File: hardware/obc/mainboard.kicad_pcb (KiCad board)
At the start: 6 copper layers, 95.9 x 90.2 mm, 213 parts, among them J101 Conn_02x20_Odd_Even, J301 USB_C_Receptacle_USB2.0, J302 Conn_High-Rel_4S2P, J303 Conn_01x06, J304 Conn_High-Rel_6P, J305 Conn_01x05, J601 Conn_01x08_Socket, J602 SMA RA Connector, J603 SMA RA Connector, J604 SMA RA Connector, Q201 BSS138DWQ-7, Q202 BSS138DWQ-7, Q203 MBT2222ADW1T1, Q204 MBT2222ADW1T1, Q205 BSS138DWQ-7, Q206 BSS138DWQ-7, Q207 MBT2222ADW1T1, Q208 MBT2222ADW1T1, Q209 MMDT2907, Q401 MBT2222ADW1T1, Q402 MBT2222ADW1T1, Q403 IRLML2803, Q404 IRF7406PbF, Q501 MMBT2222AT, Q502 IRLML2803, Q503 IRLML2803, Q504 IRLML2803, Q505 IRF7406PbF, Q506 IRF7406PbF, Q507 IRF7406PbF, U101 MAX706RESA, U102 ATSAMD51J20A-AU, U103 BMI088, U301 Mem_MT29F4G01ABAFDWB, U302 Mem_MT29F4G01ABAFDWB, U401 TPS7A4501DCQT, U402 LTC4121, U403 TPS54226PWPRPWP14_2P31X2P46-L, U404 ADM1176-1ARMZ-R7, U405 BQ25886RGER, U501 PE014006, U601 RFM98PW, U602 S1216V8, U603 GP2S1+, Y101 32.768kHz

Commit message: obc: begun formal layout
Organized the components of the first two schematic pages into formal layout and switched out connector components. Introduced step files for previously developed footprints.
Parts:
- added C118: 0.1uF, Capacitor_SMD:C_0603_1608Metric, F.Cu at (148.0, 111.6)
- added C119: 0.1uF, Capacitor_SMD:C_0603_1608Metric, F.Cu at (160.8, 105.2)
- added C120: 0.1uF, Capacitor_SMD:C_0603_1608Metric, F.Cu at (151.2, 91.6)
- J303: footprint Connector_PinHeader_2.54mm:PinHeader_1x06_P2.54mm_Vertical -> Connector_PinHeader_2.54mm:PinHeader_1x06_P2.54mm_Horizontal
- J304: footprint SSE_Footprints:Harwin_M300-MV30645M1_6P_P3.0mm_Vertical -> SSE_Footprints:MMCX-6_UMPT-06-01-L-RA-WT-TR_P2.0mm
- moved J301 222.8 mm to (250.8, 40.8), turned to 90 degrees
- moved C303 209.9 mm to (242.6, 35.5), turned to 180 degrees
- moved R307 208.4 mm to (242.5, 46.8), turned to 0 degrees
- moved R304 208.1 mm to (242.5, 41.1), turned to 0 degrees
- moved R303 208.0 mm to (242.5, 44.0), turned to 0 degrees
- moved R306 207.9 mm to (242.5, 38.4), turned to 0 degrees
- moved R112 130.0 mm to (110.8, 143.4)
- moved R231 122.9 mm to (244.0, 118.8), turned to 0 degrees
- moved R229 121.3 mm to (244.0, 115.4), turned to 0 degrees
- moved H101 120.5 mm to (191.7, 140.8), turned to 180 degrees
- moved R230 120.4 mm to (244.0, 121.6), turned to 0 degrees
- moved R110 119.8 mm to (186.8, 140.8), turned to 180 degrees
- moved H103 115.5 mm to (106.0, 143.3), turned to 180 degrees
- moved H102 114.6 mm to (191.7, 67.1), turned to 180 degrees
- moved H104 110.7 mm to (106.0, 63.3), turned to 180 degrees
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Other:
- board text added: "+X"
- board text added: "+Y"
- board text added: "+Z"

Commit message: obc: formal placement and 3D models entered
Placed components of onto board, orienting them for ease of trace creation. Entered 3D models of footprints into KiCad for design verification and aesthetics.
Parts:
- J304, U501: moved to B.Cu
- U404: value ADM1176-1ARMZ-R7 -> RM_10
- moved J302 242.0 mm to (266.4, 39.6)
- moved C304 221.1 mm to (260.4, 39.3), turned to 180 degrees
- moved C305 218.6 mm to (260.4, 42.1), turned to 180 degrees
- moved J304 161.0 mm to (207.1, 81.5), turned to -90 degrees
- moved J303 157.4 mm to (186.4, 74.5), turned to 0 degrees
- moved R510 147.0 mm to (152.8, 78.4), turned to 180 degrees
- moved JP509 146.0 mm to (142.0, 75.1), turned to 90 degrees
- moved R507 145.4 mm to (152.8, 81.2), turned to 0 degrees
- moved Q504 144.7 mm to (148.9, 79.8), turned to 180 degrees
- moved D402 143.3 mm to (194.3, 104.0), turned to 180 degrees
- moved R504 143.0 mm to (148.8, 84.0), turned to 180 degrees
- moved R430 140.9 mm to (189.8, 104.0), turned to 180 degrees
- moved Q507 139.8 mm to (142.0, 80.8), turned to 180 degrees
- moved JP508 135.0 mm to (135.0, 75.1), turned to 90 degrees
- moved JP507 130.4 mm to (127.9, 65.7), turned to 90 degrees
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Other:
- outline, holes or cut-outs redrawn

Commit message: obc: component reorganization
Blanket shrunk silk text, edited connector placement, switched out molex connectors, entered step files, and reorganized to increase area-efficiency.
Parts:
- JP501, JP502, JP503, JP504, JP505, JP506: footprint mainboard:MOLEX-1X3_LOCK -> SSE_Footprints:CONN_22-11-2032_MOL
- JP507, JP508, JP509: footprint mainboard:MOLEX-1X3_LOCK -> SSE_Footprints:CONN_22-11-2032_MOL; moved to B.Cu
- U404: value RM_10 -> ADM1176-1ARMZ-R7
- moved C601 74.2 mm to (204.4, 137.2)
- moved Q209 73.5 mm to (141.1, 119.6)
- moved R225 70.7 mm to (146.0, 125.2)
- moved R226 70.7 mm to (146.0, 122.4)
- moved R228 67.0 mm to (141.2, 126.0)
- moved R227 67.0 mm to (141.2, 123.2)
- moved U601 61.4 mm to (166.4, 129.8)
- moved C407 49.9 mm to (150.7, 171.7)
- moved L401 49.9 mm to (154.7, 171.3)
- moved U403 49.9 mm to (143.2, 172.4)
- moved C410 49.9 mm to (135.9, 172.9)
- moved C412 49.9 mm to (135.9, 170.1)
- moved R409 49.9 mm to (140.3, 166.1)
- moved R412 49.9 mm to (143.1, 166.1)
- moved R413 49.8 mm to (140.4, 182.6)
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
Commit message: obc: preliminary layout complete
Finished preliminary layout of components onto pcb. Entered revised SMA connector into design, however, there is confusion with regards to board cutouts.
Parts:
- J602, J603, J604: footprint Connector_Coaxial:SMA_Amphenol_132289_EdgeMount -> SSE_Footprints:SAMTEC_MMCXV-J-P-HF-ST-EM1
- moved J602 182.8 mm to (183.6, 116.6), turned to -90 degrees
- moved J603 180.3 mm to (183.6, 123.8), turned to -90 degrees
- moved J604 159.6 mm to (183.6, 131.2), turned to -90 degrees
- moved C304 112.4 mm to (160.8, 91.2)
- moved C305 112.3 mm to (160.8, 94.0)
- moved J302 109.2 mm to (167.8, 86.4)
- moved R229 93.8 mm to (152.8, 137.6), turned to 90 degrees
- moved R231 90.4 mm to (155.6, 137.6), turned to 90 degrees
- moved R230 87.1 mm to (158.4, 137.6), turned to 90 degrees
- moved R602 65.8 mm to (160.8, 88.4)
- moved U603 52.9 mm to (170.0, 118.3)
- moved C401 50.7 mm to (168.3, 126.4)
- moved C402 50.6 mm to (165.5, 126.4)
- moved C413 50.5 mm to (164.0, 134.3)
- moved R413 50.5 mm to (155.6, 134.3)
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
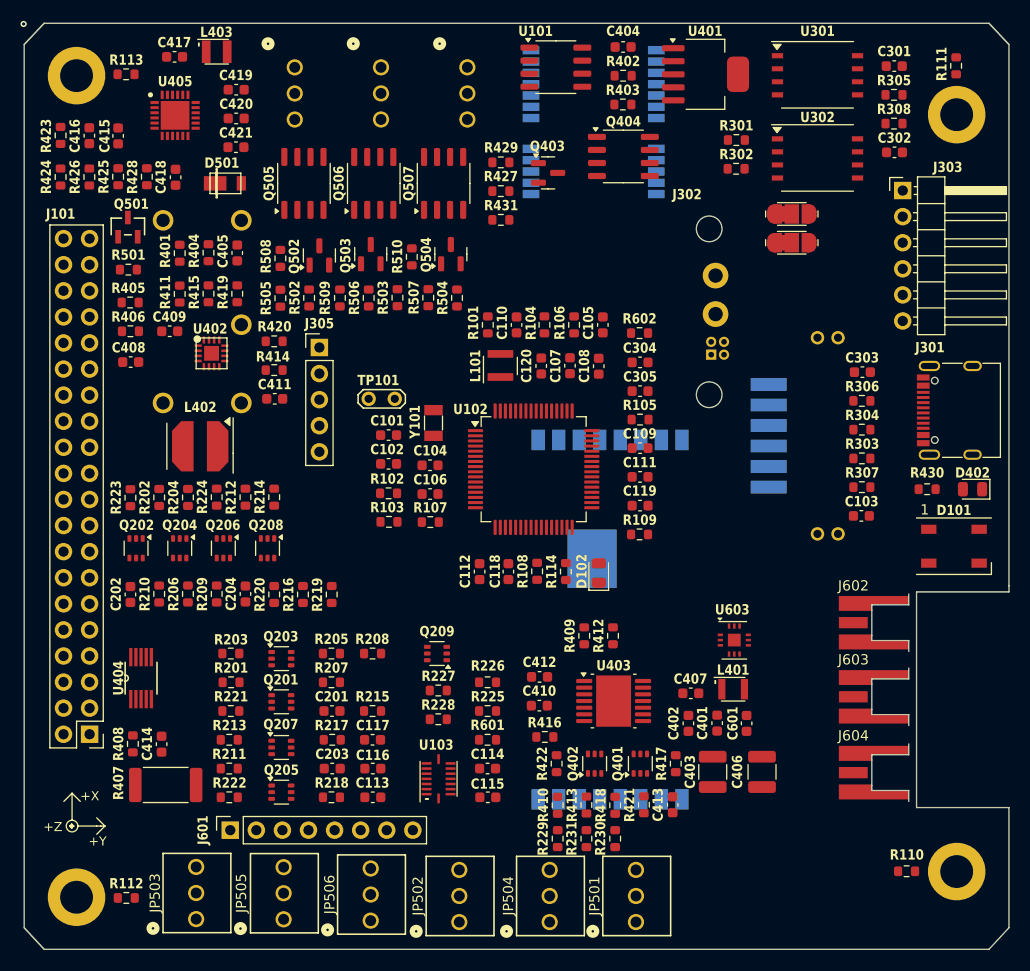
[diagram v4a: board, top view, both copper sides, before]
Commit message: obc: Update board outline and MMCXV 3d model
The model was upside down; the board edge lines were not connected.
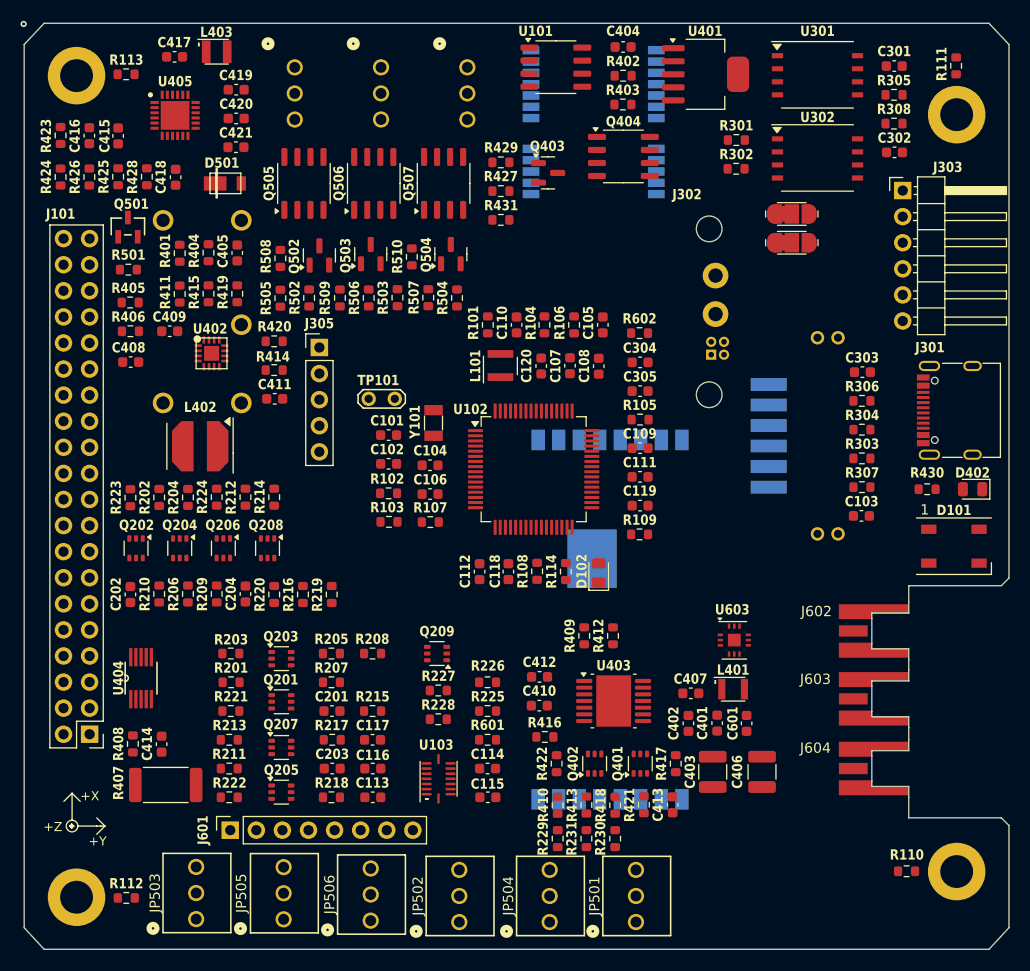
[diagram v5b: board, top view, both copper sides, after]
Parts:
- moved J602 0.80 mm to (183.6, 117.4)
- moved J604 0.40 mm to (183.6, 130.8)
- moved J603 0.20 mm to (183.6, 124.0)
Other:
- outline, holes or cut-outs redrawn
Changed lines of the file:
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@@
 	(footprint "SSE_Footprints:SAMTEC_MMCXV-J-P-HF-ST-EM1"
 		(layer "F.Cu")
-		(at 183.6 123.8125 -90)
+		(at 183.6 124.0125 -90)
 		(property "Reference" "J603"
-			(at -3.6125 2 180)
+			(at -1.9125 5.7 180)
 			(layer "F.SilkS")
 			(effects
@@
 			)
 		)
-		(property ki_fp_filters "*BNC* *SMA* *SMB* *SMC* *Cinch* *LEMO* *UMRF* *MCX* *U.FL*")
-		(sheetname "RF and GPS")
-		(sheetfile "RF_and_GPS.kicad_sch")
 		(attr smd)
 		(fp_poly
@@
 		(model "MMCXV-J-P-HF-ST-EM1.step"
 			(offset
-				(xyz 0 -0.5 0)
+				(xyz 0 -0.15 0.4)
 			)
 			(scale
@@
 			)
 			(rotate
-				(xyz 0 0 0)
+				(xyz 0 180 0)
 			)
 		)
@@
 		(tags "Through hole pin header THT 1x05 2.54mm single row")
 		(property "Reference" "J305"
-			(at 0 -2.33 360)
+			(at 0 -2.33 0)
 			(layer "F.SilkS")
 			(effects
@@
 		)
 		(property "Value" "Conn_01x05"
-			(at 0 12.49 360)
+			(at 0 12.49 0)
 			(layer "F.Fab")
 			(effects
@@
 		(tags "resistor")
 		(property "Reference" "R230"
-			(at 0 -1.43 270)
+			(at 0 -1.43 -90)
 			(layer "F.SilkS")
 			(effects
@@
 		)
 		(property "Value" "0"
-			(at 0 1.43 270)
+			(at 0 1.43 -90)
 			(layer "F.Fab")
 			(effects
@@
 		)
 		(fp_text user "${REFERENCE}"
-			(at 0 0 270)
+			(at 0 0 -90)
 			(layer "F.Fab")
 			(effects
@@
 		(tags "resistor")
 		(property "Reference" "R231"
-			(at 0 -1.43 270)
+			(at 0 -1.43 -90)
 			(layer "F.SilkS")
 			(effects
@@
 		)
 		(property "Value" "0"
-			(at 0 1.43 270)
+			(at 0 1.43 -90)
 			(layer "F.Fab")
 			(effects
@@
 		)
 		(fp_text user "${REFERENCE}"
-			(at 0 0 270)
+			(at 0 0 -90)
 			(layer "F.Fab")
 			(effects
@@
 		(tags "resistor")
 		(property "Reference" "R229"
-			(at 0 -1.43 270)
+			(at 0 -1.43 -90)
 			(layer "F.SilkS")
 			(effects
@@
 		)
 		(property "Value" "0"
-			(at 0 1.43 270)
+			(at 0 1.43 -90)
 			(layer "F.Fab")
 			(effects
@@
 		)
 		(fp_text user "${REFERENCE}"
-			(at 0 0 270)
+			(at 0 0 -90)
 			(layer "F.Fab")
 			(effects
@@
 	(footprint "SSE_Footprints:SAMTEC_MMCXV-J-P-HF-ST-EM1"
 		(layer "F.Cu")
-		(at 183.6 131.2 -90)
+		(at 183.6 130.8 -90)
 		(property "Reference" "J604"
-			(at -3.6 2 180)
+			(at -2 5.7 180)
 			(layer "F.SilkS")
 			(effects
@@
 			)
 		)
-		(property ki_fp_filters "*BNC* *SMA* *SMB* *SMC* *Cinch* *LEMO* *UMRF* *MCX* *U.FL*")
-		(sheetname "RF and GPS")
-		(sheetfile "RF_and_GPS.kicad_sch")
 		(attr smd)
 		(fp_poly
@@
 		(model "MMCXV-J-P-HF-ST-EM1.step"
 			(offset
-				(xyz 0 -0.5 0)
+				(xyz 0 -0.15 0.4)
 			)
 			(scale
@@
 			)
 			(rotate
-				(xyz 0 0 0)
+				(xyz 0 180 0)
 			)
 		)
@@
 	(footprint "SSE_Footprints:SAMTEC_MMCXV-J-P-HF-ST-EM1"
 		(layer "F.Cu")
-		(at 183.6 116.6 -90)
+		(at 183.6 117.4 -90)
 		(property "Reference" "J602"
-			(at -3.6 2 180)
+			(at -1.9 5.6 180)
 			(layer "F.SilkS")
 			(effects
@@
 			)
 		)
-		(property ki_fp_filters "*BNC* *SMA* *SMB* *SMC* *Cinch* *LEMO* *UMRF* *MCX* *U.FL*")
-		(sheetname "RF and GPS")
-		(sheetfile "RF_and_GPS.kicad_sch")
 		(attr smd)
 		(fp_poly
@@
 		(model "MMCXV-J-P-HF-ST-EM1.step"
 			(offset
-				(xyz 0 -0.5 0)
+				(xyz 0 -0.15 0.4)
 			)
 			(scale
@@
 			)
 			(rotate
-				(xyz 0 0 0)
+				(xyz 0 180 0)
 			)
 		)
@@
 		(tags "resistor")
 		(property "Reference" "R602"
-			(at 0 -1.4 360)
+			(at 0 -1.4 0)
 			(layer "F.SilkS")
 			(effects
@@
 		)
 		(property "Value" "10k"
-			(at 0 1.43 360)
+			(at 0 1.43 0)
 			(layer "F.Fab")
 			(effects
@@
 		)
 		(fp_text user "${REFERENCE}"
-			(at 0 0 360)
+			(at 0 0 0)
 			(layer "F.Fab")
 			(effects
@@
 		(at 158.4 116.4 90)
 		(property "Reference" "U601"
-			(at 1.016 2.667 270)
+			(at 1.016 2.667 -90)
 			(layer "B.SilkS")
 			(hide yes)
@@
 		)
 		(property "Value" "RFM98PW"
-			(at -4.318 -7.6835 270)
+			(at -4.318 -7.6835 -90)
 			(layer "B.SilkS")
 			(hide yes)
@@
 		)
 		(fp_text user "RADIO 2"
-			(at 5.08 6.1595 270)
+			(at 5.08 6.1595 -90)
 			(layer "B.SilkS")
 			(hide yes)
@@
 	)
 	(gr_line
-		(start 196.745 134.6)
+		(start 196.745 136.345)
 		(end 196.745 146.3)
 		(stroke
@@
 	)
 	(gr_line
+		(start 186.99 133.6)
+		(end 186.99 135.6)
+		(stroke
+			(width 0.1)
+			(type default)
+		)
+		(layer "Edge.Cuts")
+	)
+	(gr_line
 		(start 100.855 146.3)
 		(end 100.855 60.3)
@@
 	(gr_line
 		(start 102.8 148.4)
-		(end 100.855 146.3)
+		(end 100.854984 146.300015)
 		(stroke
-			(width 0.15)
+			(width 0.1)
 			(type default)
 		)
@@
 	)
 	(gr_line
-		(start 187.745 134.6)
-		(end 187.745 113.6)
+		(start 186.99 113)
+		(end 186.99 114.6)
 		(stroke
 			(width 0.1)
@@
 	)
 	(gr_line
-		(start 187.745 113.6)
-		(end 196.745 113.6)
+		(start 186.99 113)
+		(end 196 113)
 		(stroke
 			(width 0.1)
@@
 	(gr_line
 		(start 196.745 60.3)
-		(end 196.745 113)
+		(end 196.745 112.255)
+		(stroke
+			(width 0.1)
+			(type default)
+		)
+		(layer "Edge.Cuts")
+	)
+	(gr_line
+		(start 186.99 126.8125)
+		(end 186.99 128)
 		(stroke
 			(width 0.1)
@@
 	)
 	(gr_line
-		(start 187.745 134.6)
-		(end 196.745 134.6)
+		(start 186.99 135.6)
+		(end 196 135.6)
+		(stroke
+			(width 0.1)
+			(type default)
+		)
+		(layer "Edge.Cuts")
+	)
+	(gr_line
+		(start 196 113)
+		(end 196.745 112.255)
 		(stroke
 			(width 0.1)
@@
 		(end 102.8 58.23)
 		(stroke
-			(width 0.15)
+			(width 0.1)
+			(type default)
+		)
+		(layer "Edge.Cuts")
+	)
+	(gr_line
+		(start 196.745 136.345)
+		(end 196 135.6)
+		(stroke
+			(width 0.1)
 			(type default)
 		)
@@
 	)
 	(gr_line
-		(start 196.745 60.3)
-		(end 194.8 58.23)
+		(start 186.99 120.2)
+		(end 186.99 121.2125)
 		(stroke
-			(width 0.15)
+			(width 0.1)
 			(type default)
 		)
@@
 	)
 	(gr_line
-		(start 196.745 113)
-		(end 196.745 113.6)
+		(start 196.745 60.3)
+		(end 194.8 58.23)
 		(stroke
 			(width 0.1)

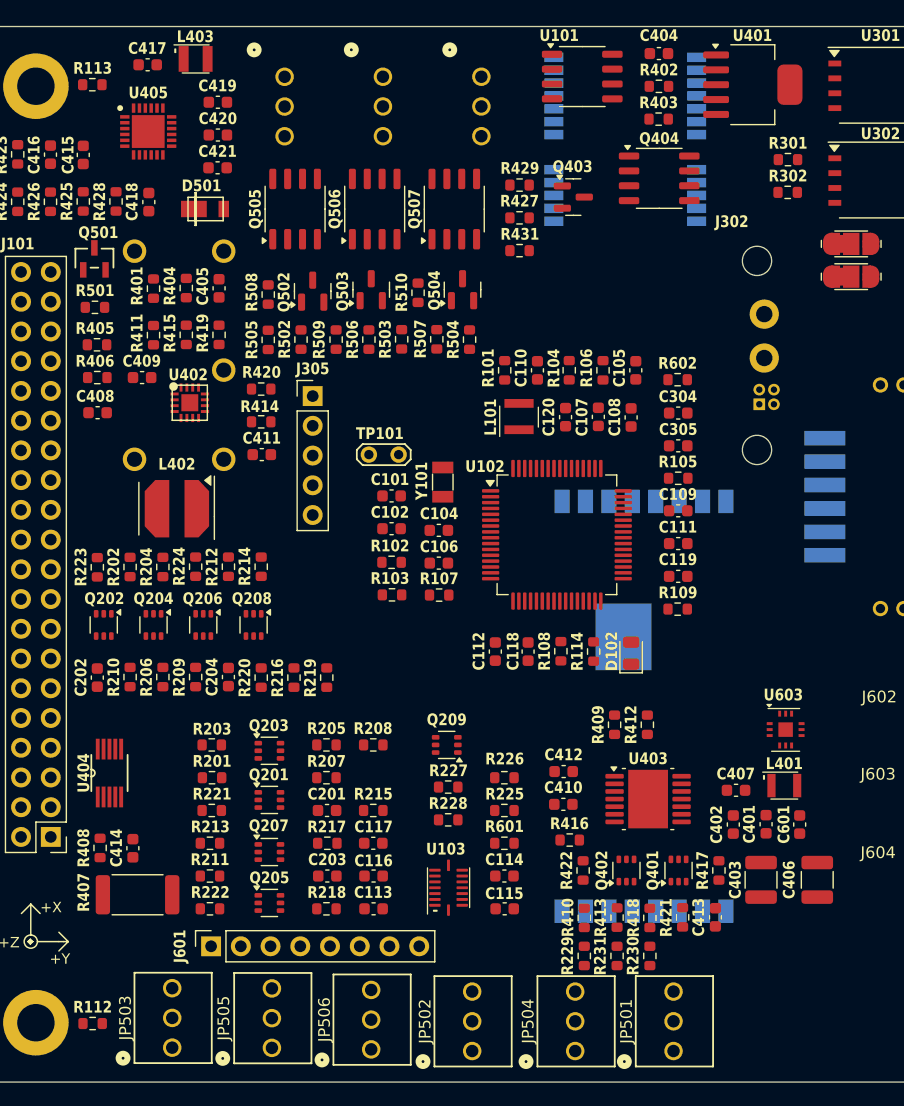
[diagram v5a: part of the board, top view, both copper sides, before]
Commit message: obc: design review 5/28 implemented
Entered step models, adjusted pin clearances, and edited footprints.
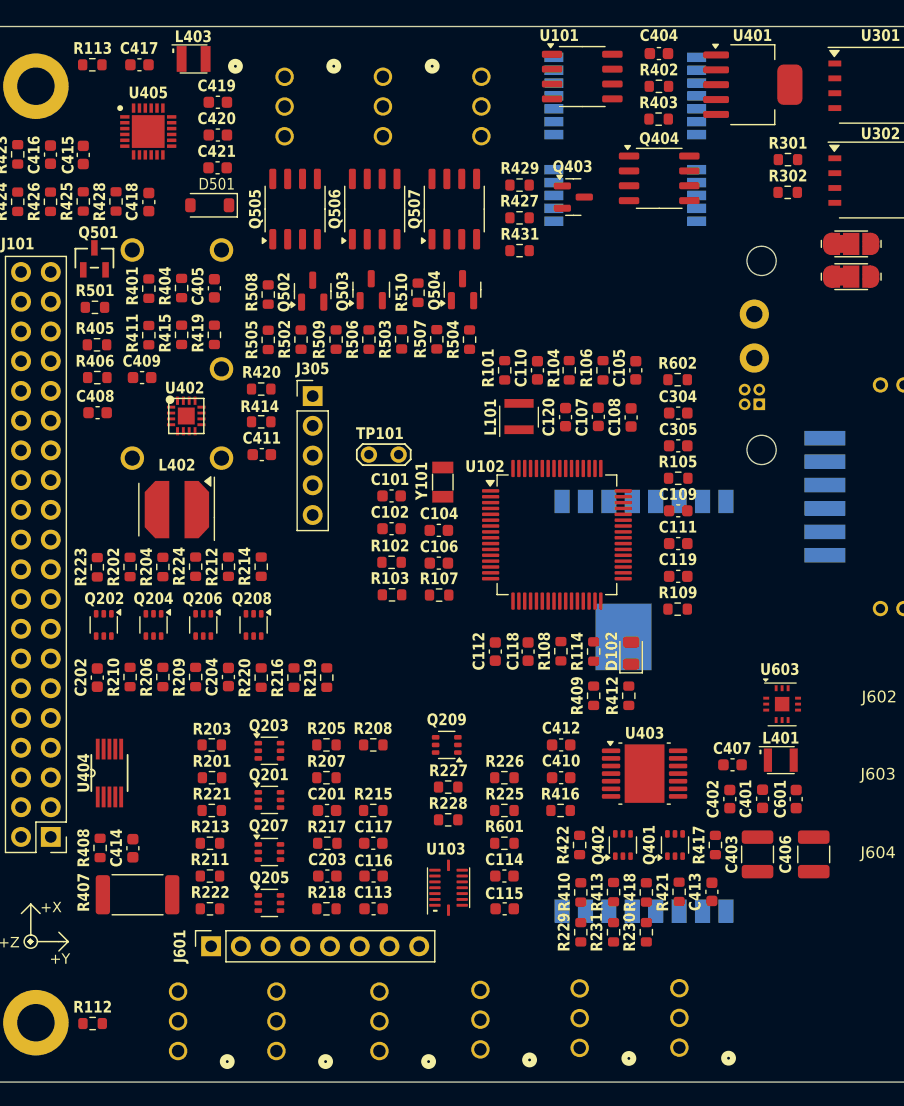
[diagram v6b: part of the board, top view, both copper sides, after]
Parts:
- D501: footprint mainboard:PWRDI-123 -> Diode_SMD:D_SOD-123
- J302, JP501, JP502, JP503, JP504, JP505, JP506: moved to B.Cu
- U501: footprint mainboard:RELAY_PE014006 -> SSE_Footprints:RELAY_PE014006_REV-SSE
- moved JP503 43.3 mm to (160.9, 145.5)
- moved JP501 42.3 mm to (118.1, 145.7)
- moved JP505 26.3 mm to (152.4, 145.5)
- moved JP504 25.5 mm to (126.5, 145.7)
- moved U501 10.6 mm to (117.8, 84.6)
- moved JP506 9.33 mm to (143.9, 145.6)
- moved JP502 7.92 mm to (135.3, 145.7)
- moved R409 3.05 mm to (153.6, 115.4)
- moved R412 2.94 mm to (156.6, 115.4)
- moved R416 2.64 mm to (150.8, 125.2)
- moved C412 2.28 mm to (150.8, 119.6)
- moved C410 2.28 mm to (150.8, 122.4)
- moved C402 2.20 mm to (165.2, 124.2)
- moved C403 2.20 mm to (167.6, 128.9)
- moved R410 2.20 mm to (152.5, 132.2)
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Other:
- board text added: "D501"
